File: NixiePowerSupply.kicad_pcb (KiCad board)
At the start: 2 copper layers, 50.8 x 44.4 mm, 21 parts, among them J1 BARREL_JACK, P1 CONN_01X03, P2 CONN_01X02, T1 IRF644, U1 MAX1771

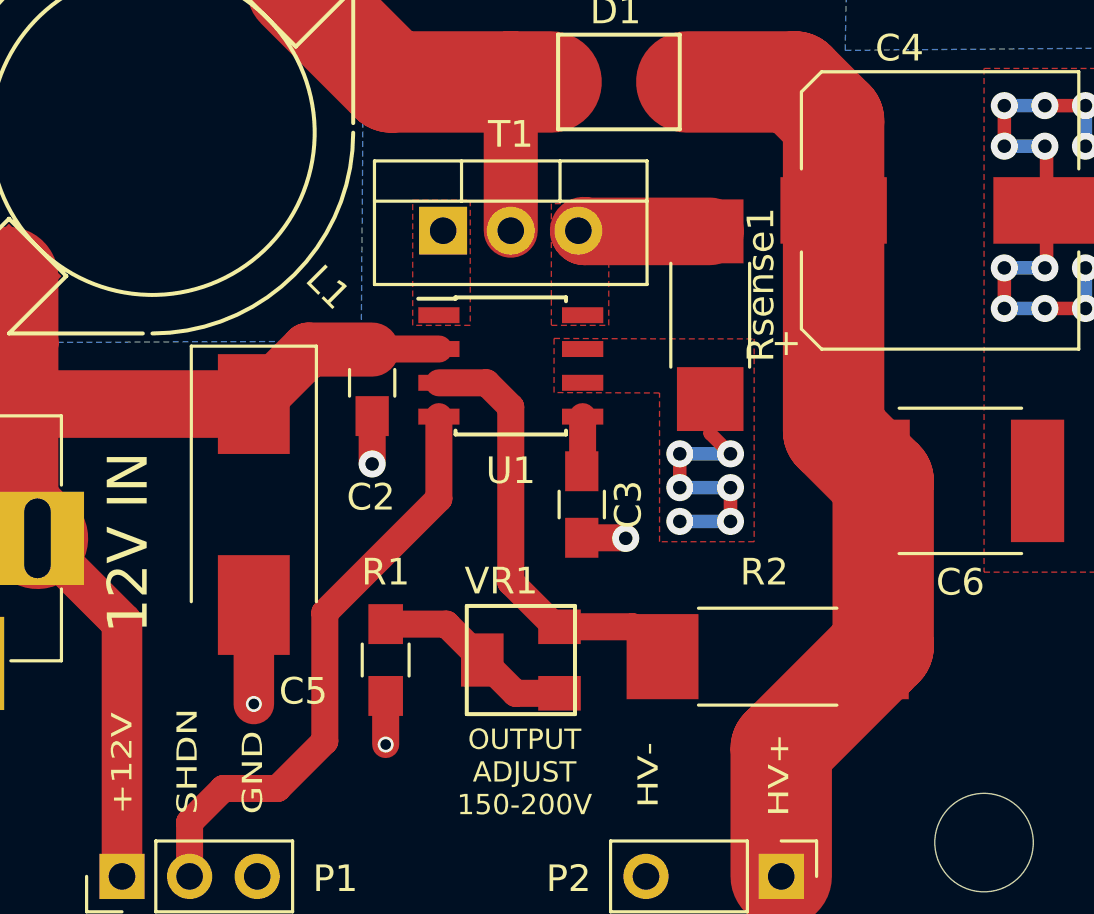
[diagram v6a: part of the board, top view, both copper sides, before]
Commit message: Add barrel jack model
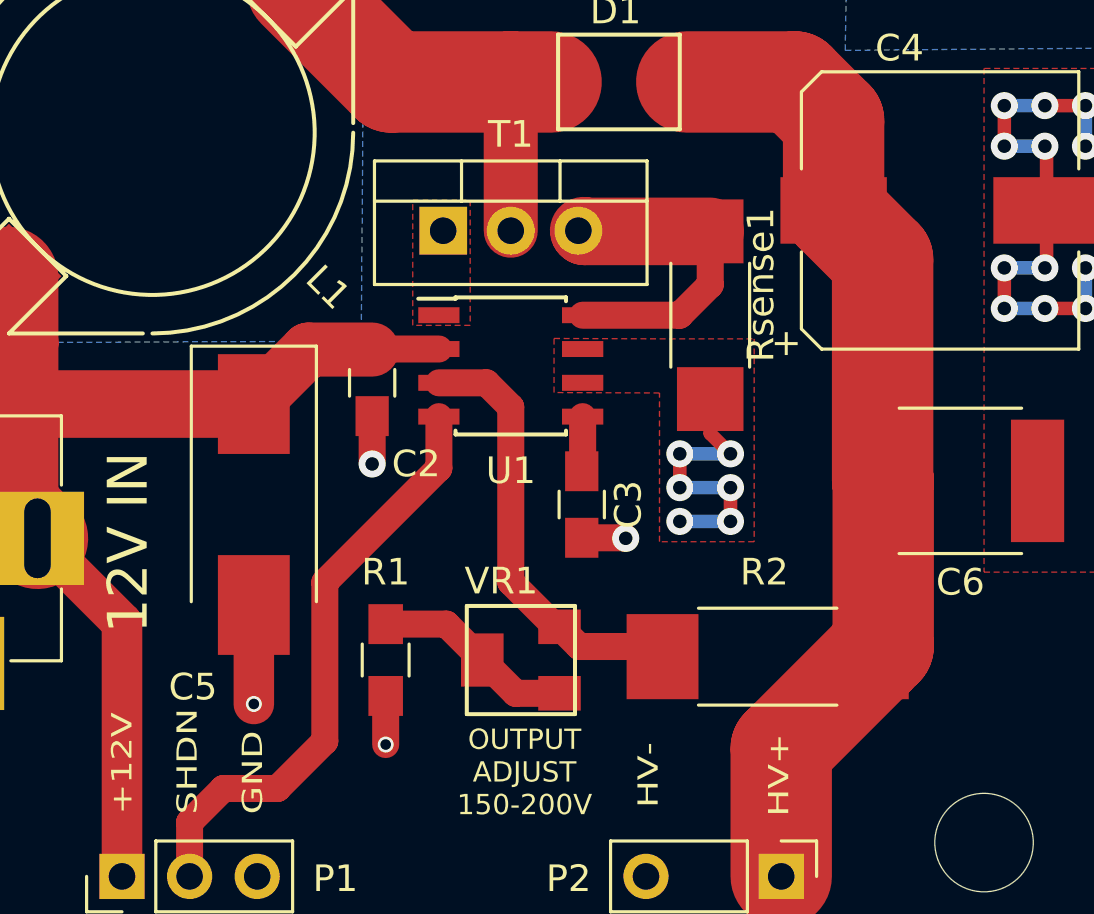
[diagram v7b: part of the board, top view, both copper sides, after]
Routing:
- net Net-(Rsense1-Pad1): track 4.76 -> 12.0 mm
- removed copper zone on F.Cu, net Net-(Rsense1-Pad1)
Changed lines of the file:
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@@
-(kicad_pcb (version 4) (host pcbnew 4.0.5)
+(kicad_pcb (version 4) (host pcbnew 4.0.6)
   (general
     (links 34)
     (no_connects 0)
-    (area 40.384999 24.805 99.568572 72.195)
+    (area 44.399999 25.349999 95.300001 69.900001)
     (thickness 1.6)
     (drawings 9)
-    (tracks 100)
+    (tracks 105)
     (zones 0)
     (modules 21)
@@
   )
   (setup
-    (last_trace_width 0.25)
+    (last_trace_width 1.016)
     (user_trace_width 0.508)
     (user_trace_width 1.016)
@@
     (pad 3 thru_hole rect (at -3 4.7) (size 3.5 3.5) (drill oval 3 1) (layers *.Cu *.Mask)
       (net 1 GND))
+    (model ${KIPRJMOD}/models/AB2_PB_2MM_JACK_PTH.wrl
+      (at (xyz -0.48 0 0))
+      (scale (xyz 0.38 0.34 0.36))
+      (rotate (xyz 0 0 90))
+    )
   )
   (module Resistors_SMD:R_0805_HandSoldering (layer F.Cu)
@@
     (pad 2 smd rect (at 1.45 1.25) (size 1.6 1.3) (layers F.Cu F.Paste F.Mask)
       (net 5 "Net-(R1-Pad1)"))
-    (model "/Users/carl/Documents/KiCad/NixiePowerSupply/models/Bourns 3214W.wrl"
+    (model "${KIPRJMOD}/models/Bourns 3214W.wrl"
       (at (xyz 0.065 -0.01 0.11))
       (scale (xyz 0.3937 0.3937 0.3937))
@@
     (tags "capacitor 0805")
     (attr smd)
-    (fp_text reference C2 (at 4.29768 0.04572 360) (layer F.SilkS)
+    (fp_text reference C2 (at 3.048 -1.651 360) (layer F.SilkS)
       (effects (font (size 1 1) (thickness 0.15)))
     )
@@
     (tags "capacitor tantalum smd")
     (attr smd)
-    (fp_text reference C5 (at 7.01548 -1.85928 360) (layer F.SilkS)
+    (fp_text reference C5 (at 6.858 2.286 360) (layer F.SilkS)
       (effects (font (size 1 1) (thickness 0.15)))
     )
@@
   (segment (start 75.09 48.768) (end 75.09 50.787) (width 1.016) (layer F.Cu) (net 2))
   (segment (start 75.09 50.787) (end 75.057 50.82) (width 1.016) (layer F.Cu) (net 2))
+  (segment (start 84.519 41.021) (end 86.36 42.862) (width 3.81) (layer F.Cu) (net 3))
+  (segment (start 86.36 42.862) (end 86.36 51.16) (width 3.81) (layer F.Cu) (net 3))
+  (segment (start 86.36 51.16) (end 86.381 51.181) (width 3.81) (layer F.Cu) (net 3))
   (segment (start 82.55 66.04) (end 82.55 61.227) (width 3.81) (layer F.Cu) (net 3))
   (segment (start 82.55 61.227) (end 85.992 57.785) (width 3.81) (layer F.Cu) (net 3))
   (segment (start 86.381 51.181) (end 86.381 57.396) (width 3.81) (layer F.Cu) (net 3))
   (segment (start 86.381 57.396) (end 85.992 57.785) (width 3.81) (layer F.Cu) (net 3))
-  (segment (start 84.519 41.021) (end 84.519 49.319) (width 3.81) (layer F.Cu) (net 3))
-  (segment (start 84.519 49.319) (end 86.381 51.181) (width 3.81) (layer F.Cu) (net 3))
   (segment (start 79.002 36.195) (end 83.066 36.195) (width 3.81) (layer F.Cu) (net 3))
   (segment (start 83.066 36.195) (end 84.519 37.648) (width 3.81) (layer F.Cu) (net 3))
@@
   (segment (start 74.221 59.162) (end 72.571 59.162) (width 1.016) (layer F.Cu) (net 5))
   (segment (start 72.571 59.162) (end 71.321 57.912) (width 1.016) (layer F.Cu) (net 5))
+  (segment (start 74.221 56.662) (end 74.963 57.404) (width 1.016) (layer F.Cu) (net 6))
+  (segment (start 74.963 57.404) (end 77.711 57.404) (width 1.016) (layer F.Cu) (net 6))
+  (segment (start 77.711 57.404) (end 78.092 57.785) (width 1.016) (layer F.Cu) (net 6))
   (segment (start 72.39 54.981) (end 72.39 48.407) (width 1.016) (layer F.Cu) (net 6))
   (segment (start 72.39 48.407) (end 71.481 47.498) (width 1.016) (layer F.Cu) (net 6))
@@
   (segment (start 74.221 56.662) (end 74.071 56.662) (width 1.016) (layer F.Cu) (net 6))
   (segment (start 74.071 56.662) (end 72.39 54.981) (width 1.016) (layer F.Cu) (net 6))
-  (segment (start 74.221 56.662) (end 76.969 56.662) (width 1.016) (layer F.Cu) (net 6))
-  (segment (start 76.969 56.662) (end 78.092 57.785) (width 1.016) (layer F.Cu) (net 6))
+  (segment (start 75.09 44.958) (end 78.74 44.958) (width 1.016) (layer F.Cu) (net 7))
+  (segment (start 78.74 44.958) (end 79.883 43.815) (width 1.016) (layer F.Cu) (net 7))
+  (segment (start 79.883 43.815) (end 79.883 41.808) (width 1.016) (layer F.Cu) (net 7))
   (segment (start 79.883 41.808) (end 75.15501 41.808) (width 2.54) (layer F.Cu) (net 7))
   (segment (start 75.15501 41.808) (end 75.13001 41.783) (width 2.54) (layer F.Cu) (net 7))
@@
   (segment (start 53.490349 52.220349) (end 54.61 53.34) (width 3.81) (layer F.Cu) (net 9))
   (segment (start 60.325 66.04) (end 60.325 64.008) (width 1.016) (layer F.Cu) (net 10))
-  (segment (start 63.627 62.738) (end 65.405 60.96) (width 1.016) (layer F.Cu) (net 10))
   (segment (start 60.325 64.008) (end 61.595 62.738) (width 1.016) (layer F.Cu) (net 10))
   (segment (start 61.595 62.738) (end 63.627 62.738) (width 1.016) (layer F.Cu) (net 10))
-  (segment (start 65.405 60.96) (end 65.405 56.134) (width 1.016) (layer F.Cu) (net 10))
-  (segment (start 65.405 56.134) (end 69.69 51.849) (width 1.016) (layer F.Cu) (net 10))
-  (segment (start 69.69 51.849) (end 69.69 48.768) (width 1.016) (layer F.Cu) (net 10))
+  (segment (start 63.627 62.738) (end 65.405 60.96) (width 1.016) (layer F.Cu) (net 10))
+  (segment (start 65.405 60.96) (end 65.405 54.991) (width 1.016) (layer F.Cu) (net 10))
+  (segment (start 65.405 54.991) (end 69.69 50.706) (width 1.016) (layer F.Cu) (net 10))
+  (segment (start 69.69 50.706) (end 69.69 48.768) (width 1.016) (layer F.Cu) (net 10))
   (zone (net 1) (net_name GND) (layer B.Cu) (hatch edge 0.508)
     (connect_pads (clearance 0.254))
@@
       )
     )
-  )
-  (zone (net 7) (net_name "Net-(Rsense1-Pad1)") (layer F.Cu) (hatch edge 0.508)
-    (connect_pads yes (clearance 0.254))
-    (min_thickness 0.254)
-    (fill yes (arc_segments 16) (thermal_gap 0.508) (thermal_bridge_width 0.508) (smoothing chamfer) (radius 0.254))
-    (polygon
-      (pts
-        (xy 76.073 45.339) (xy 76.073 40.767) (xy 73.914 40.767) (xy 73.914 45.339)
-      )
-    )
